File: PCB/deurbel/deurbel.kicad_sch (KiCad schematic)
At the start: 17 parts, among them J1 Mute, J2 Doorbell, J3 Test_Doorbell, J5 Gong, K2 SRD-05VDC-SL-C, Q1 2N7000, Q2 BC338

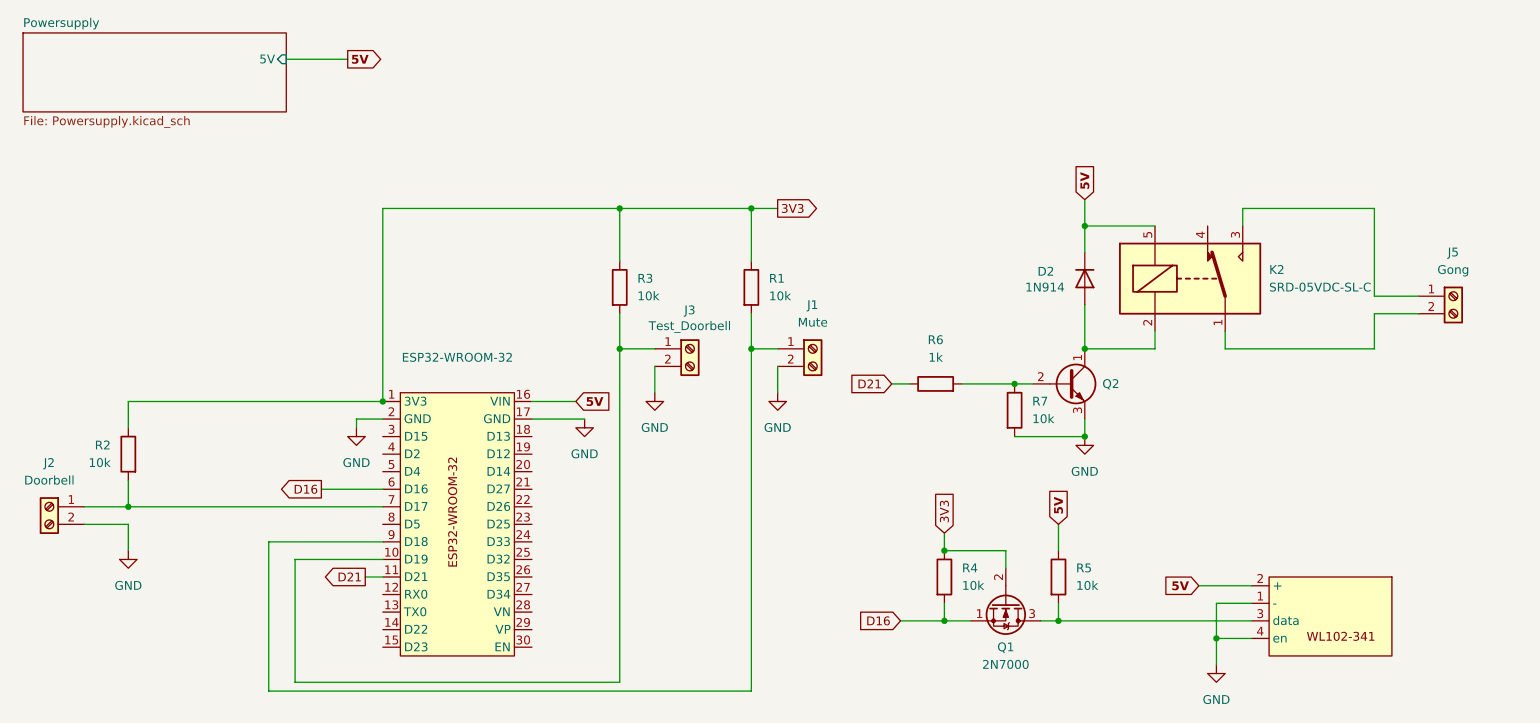
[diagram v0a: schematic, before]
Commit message: Client config is now done once and removed scanning from connection task
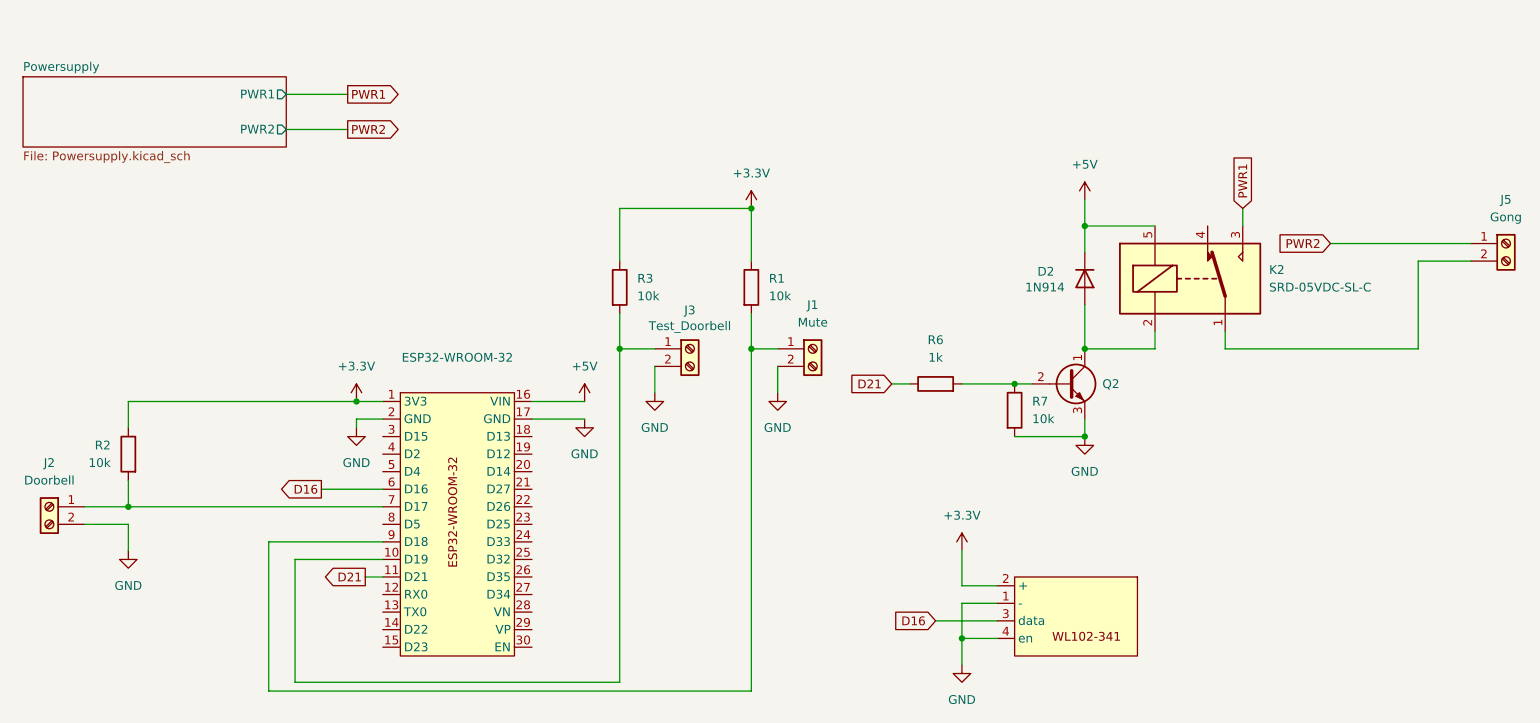
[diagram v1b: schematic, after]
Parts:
- removed Q1: 2N7000, Package_TO_SOT_THT:TO-92_Inline, symbol Transistor_FET:2N7000
- removed R4, R5: 10k, Resistor_THT:R_Axial_DIN0204_L3.6mm_D1.6mm_P5.08mm_Horizontal, symbol Device:R
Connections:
- net D16: now also WL102-1.3 (data)
- net PWR1: now reaches K2.3
- net PWR1: no longer J5.1 (Pin_1)
- net 3V3 renamed +3.3V
- net +3.3V: now also WL102-1.2 (+)
- net 5V renamed +5V
- net +5V: no longer WL102-1.2 (+)
- new net PWR2: J5.1 (Pin_1)
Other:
- sheet Powersupply ports: added PWR1, PWR2; removed 5V
- moved on the sheet: J5
